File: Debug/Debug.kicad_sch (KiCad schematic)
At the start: 37 parts, among them J1 Expansion_Connector, SW1 Step, SW2 PHI1/Step, SW4 SI/SC, U1 74HCT04, U10 MC14495P1, U11 HDSP-7803, U12 MC14495P1, U13 HDSP-7803, U14 MC14495P1, U15 HDSP-7803, U2 74HCT74, U3 MC14495P1, U4 HDSP-7803, U5 74HCT374, U6 MC14495P1, U7 HDSP-7803, U8 MC14495P1, U9 HDSP-7803

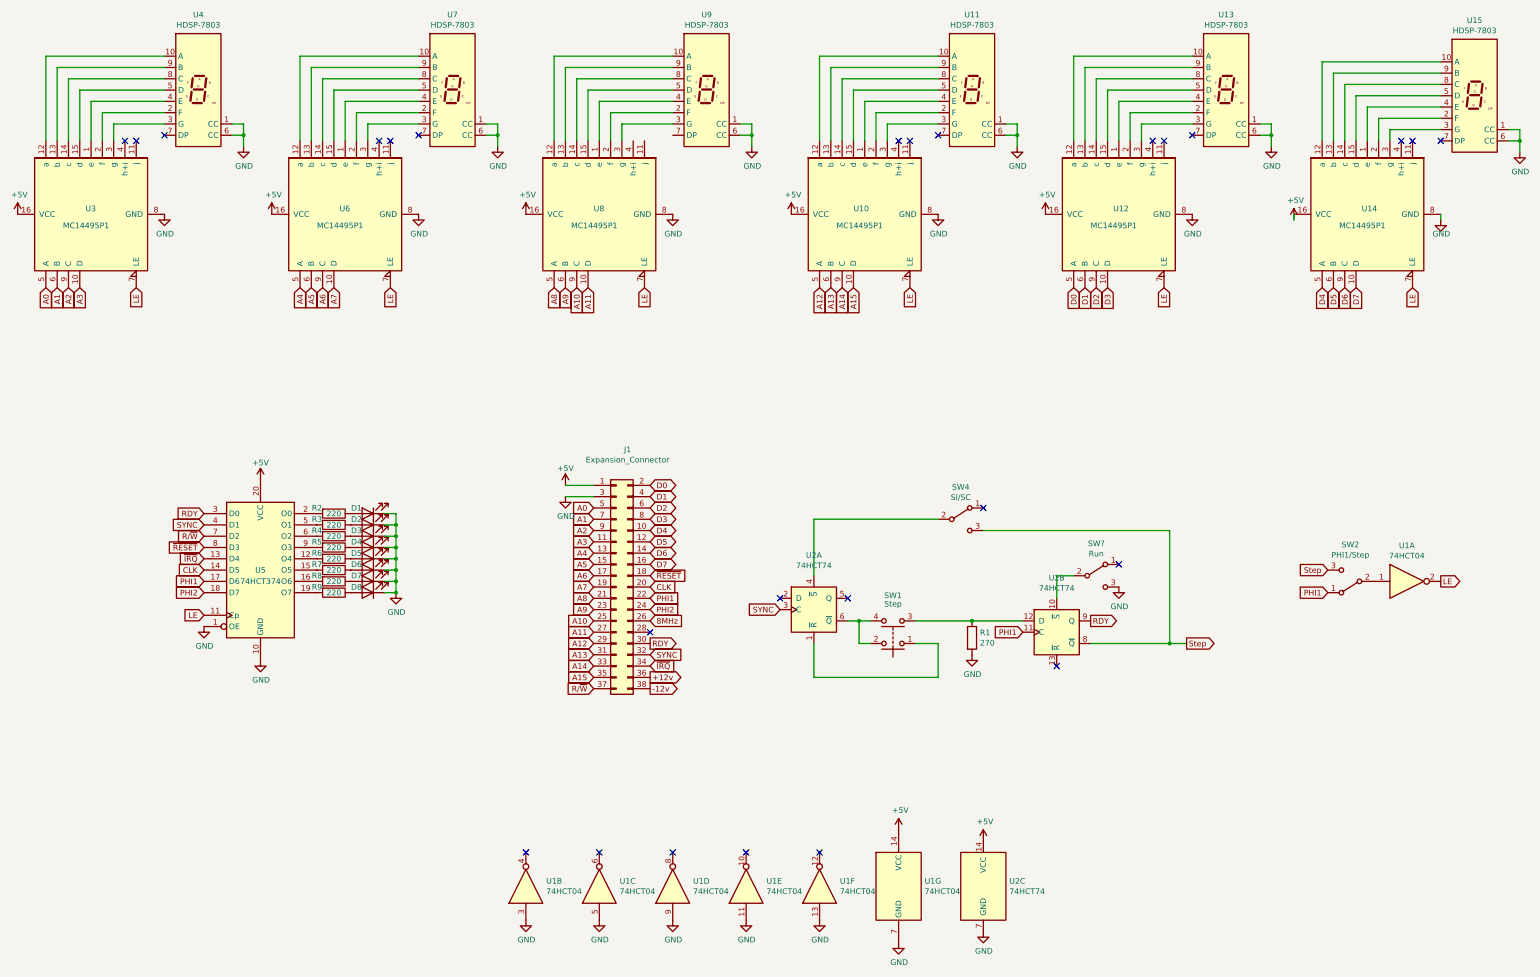
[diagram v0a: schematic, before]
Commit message: Update to latest KiCad version and other edits.
Updated the files formatting to conform to KiCad 10 standards, updated dates and corrected company name, also first signed commit to this repository.
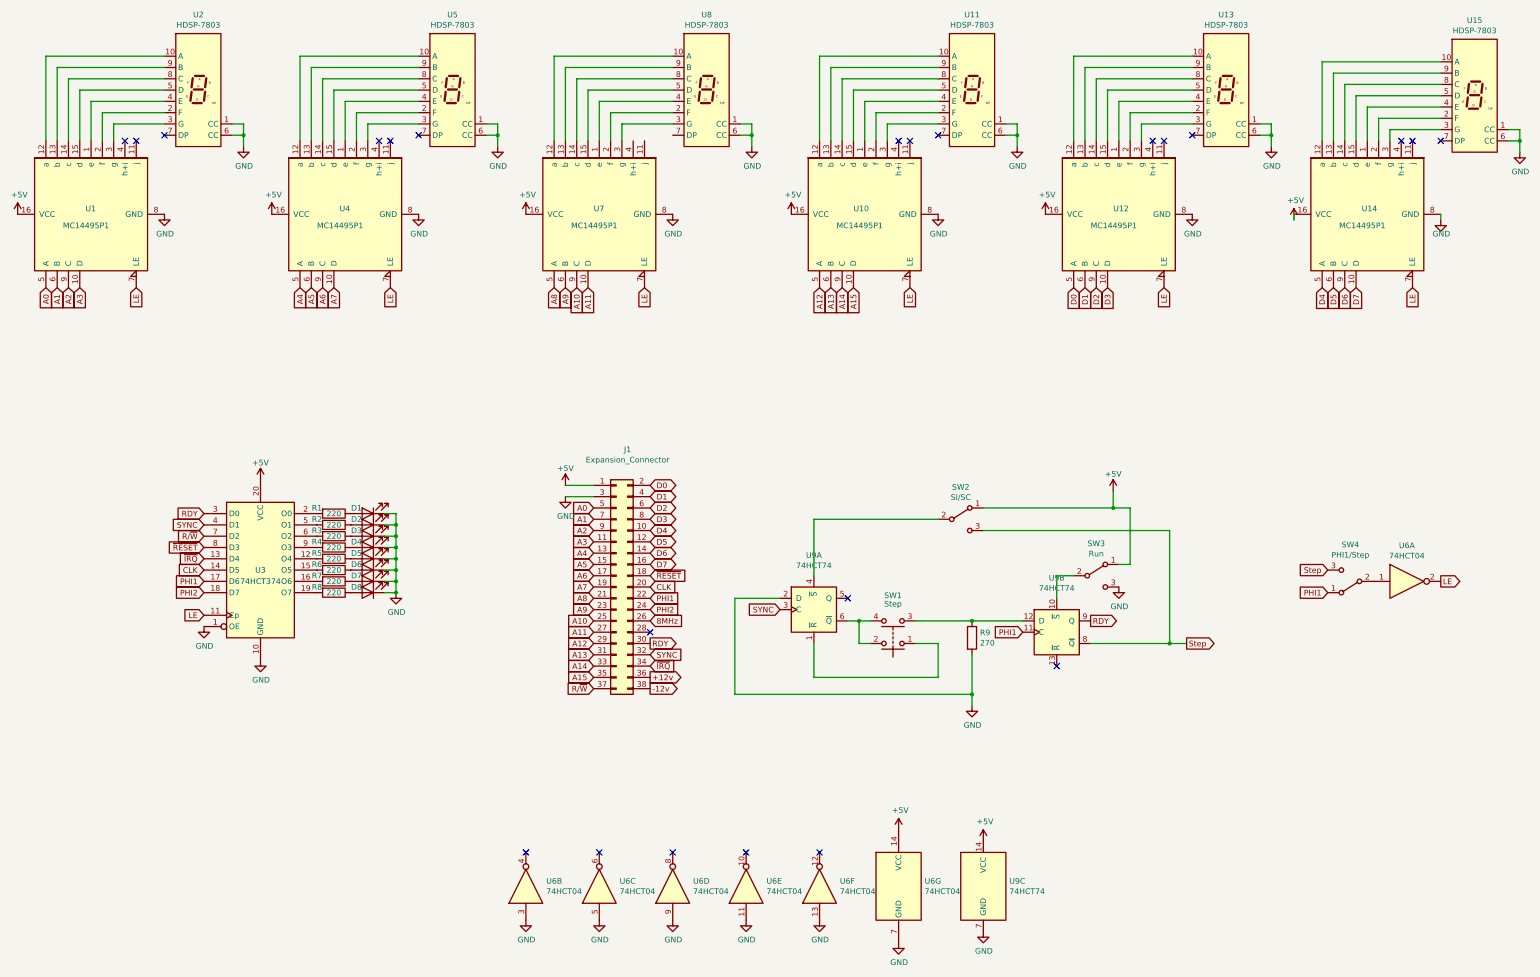
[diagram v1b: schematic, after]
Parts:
- gave numbers to parts that had none: 1
- renumbered R2 to R1, R3 to R2, R4 to R3, R5 to R4, R6 to R5, R7 to R6, R8 to R7, R9 to R8, R1 to R9, SW4 to SW2, SW2 to SW4, U3 to U1, U4 to U2, U5 to U3, U6 to U4, U7 to U5, U1 to U6, U8 to U7, U9 to U8, U2 to U9
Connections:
- net +5V: now also SW2.1 (A), SW3.1 (A)
- net GND: now also U9.2 (D)
- no-connect marks 26 -> 23
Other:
- company: WolfNet Computing -> WolfNet Computing C.I.C.
